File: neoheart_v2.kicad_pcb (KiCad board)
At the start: 2 copper layers, 54.2 x 46.5 mm, 45 parts, among them J1 Conn_01x03, Q1 A1SHB, Q2 BSS138, U2 TPS61240TDRVRQ1

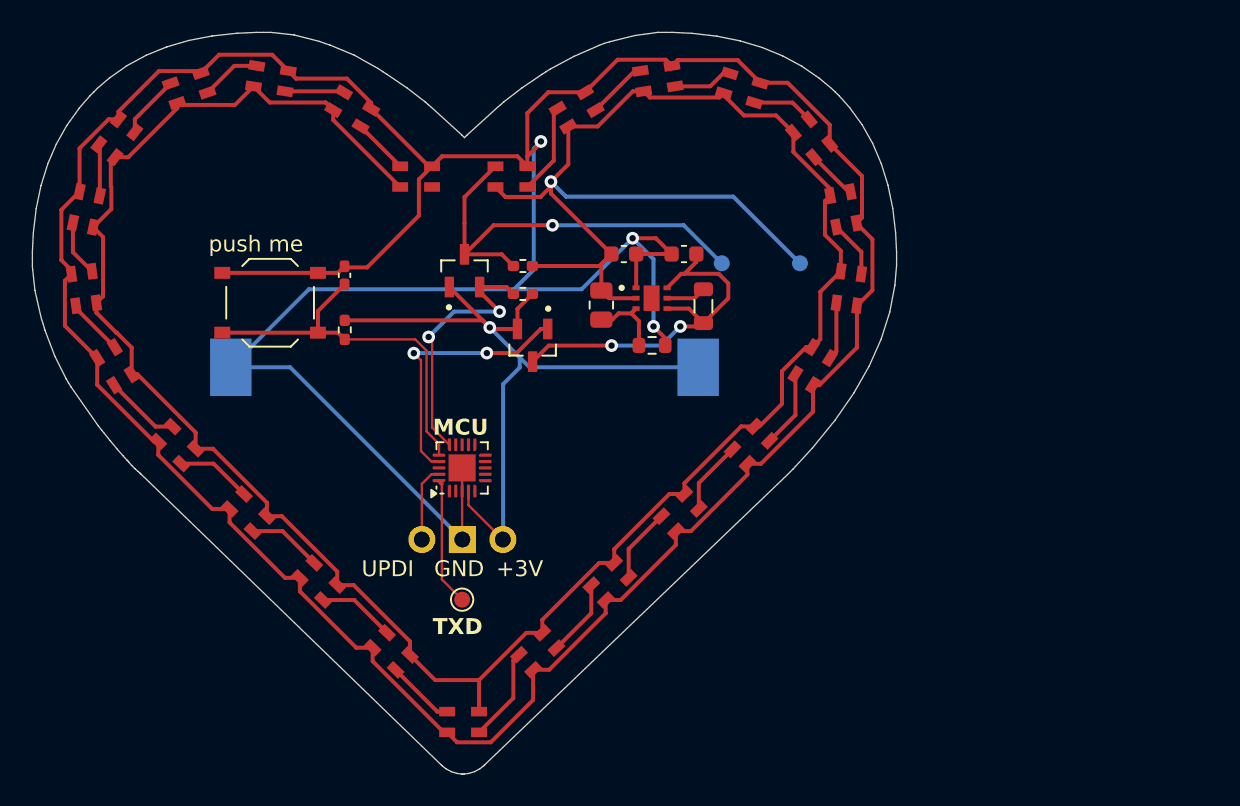
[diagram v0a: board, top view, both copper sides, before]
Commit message: 2.2: update schematic, new boost converter design, hardware optimizations
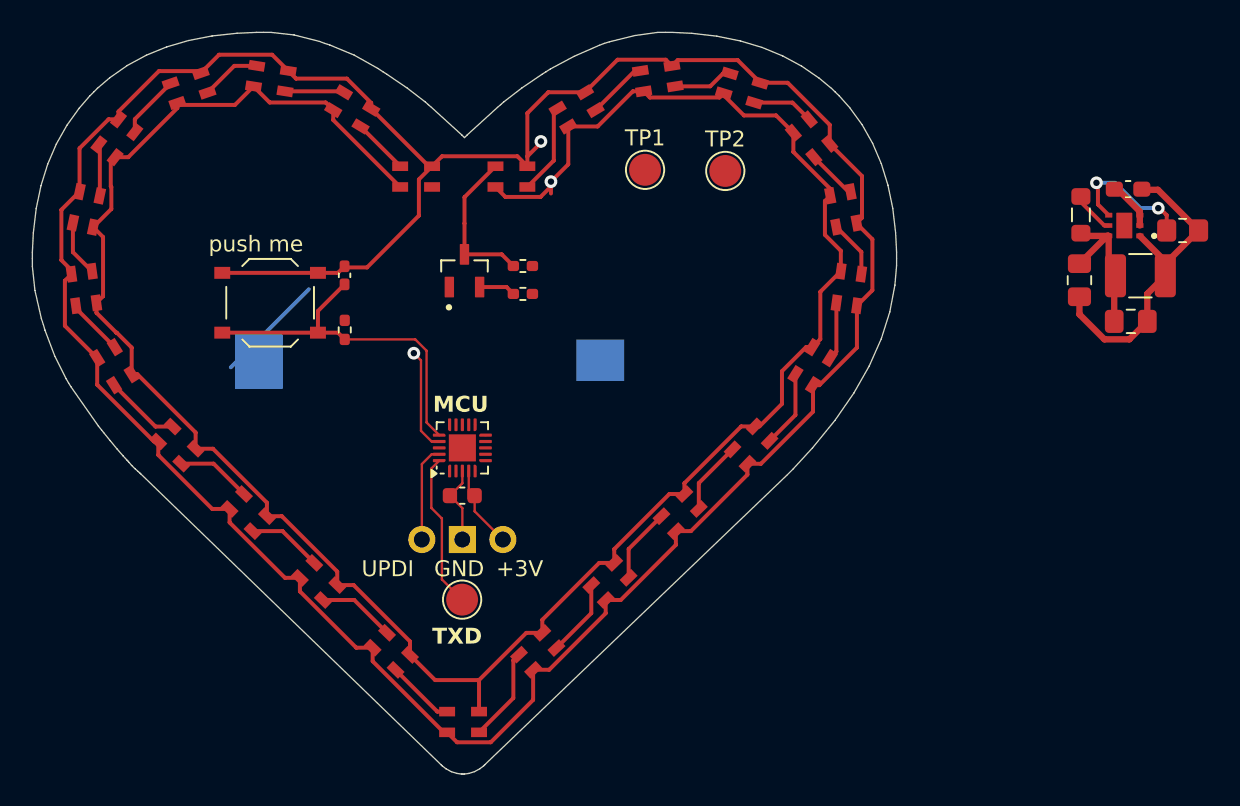
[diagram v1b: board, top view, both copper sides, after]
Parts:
- removed BT1: Battery, Battery:BatteryHolder_Keystone_1060_1x2032
- removed Q1: A1SHB, lib:SOT95P237X112-3N
- removed R2: 180kΩ, Resistor_SMD:R_0805_2012Metric
- removed R3: 1,5MΩ, Resistor_SMD:R_0603_1608Metric
- removed REF**: OSHW-Logo_5.7x6mm_SilkScreen, Symbol:OSHW-Logo_5.7x6mm_SilkScreen
- added C1: 100µF, Capacitor_SMD:C_1210_3225Metric_Pad1.33x2.70mm_HandSolder, F.Cu at (92.7, 41.4)
- added C5: 2.2µF, Capacitor_SMD:C_0805_2012Metric_Pad1.18x1.45mm_HandSolder, F.Cu at (92.1, 44.3)
- added C6: 100nF, Capacitor_SMD:C_0603_1608Metric, F.Cu at (50.2, 55.2)
- added J2: CR2032, lib:HARWIN_S8421-45R, B.Cu at (50.3, 46.7)
- added R6: 100K, Resistor_SMD:R_0805_2012Metric_Pad1.20x1.40mm_HandSolder, F.Cu at (95.3, 38.6)
- C3: footprint Capacitor_SMD:C_0603_1608Metric -> Capacitor_SMD:C_0805_2012Metric_Pad1.18x1.45mm_HandSolder
- C4: footprint Capacitor_SMD:C_0603_1608Metric -> Capacitor_SMD:C_0603_1608Metric_Pad1.08x0.95mm_HandSolder
- L1: value MLP2012V4R7MT0S1 -> 1μH; footprint Inductor_SMD:L_0805_2012Metric -> Inductor_SMD:L_0805_2012Metric_Pad1.05x1.20mm_HandSolder
- TP1, TP2: footprint TestPoint:TestPoint_Pad_D1.0mm -> TestPoint:TestPoint_Pad_D2.0mm; moved to F.Cu
- TP4: footprint TestPoint:TestPoint_Pad_D1.0mm -> TestPoint:TestPoint_Pad_D2.0mm
- U2: value TPS61240TDRVRQ1 -> TPS61240
- moved C4 31.9 mm to (91.9, 36.0)
- moved U2 30.0 mm to (91.7, 38.3), turned to 180 degrees
- moved C3 24.9 mm to (88.9, 41.7), turned to -90 degrees
- moved L1 24.4 mm to (89.0, 37.6)
- moved TP1 7.58 mm to (61.6, 34.8), turned to 0 degrees
- moved TP2 7.45 mm to (66.7, 34.9), turned to 0 degrees
- moved MCU1 1.26 mm to (50.2, 52.2)
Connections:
- C3 pad 1: /BOOST_3V0 -> +3V0
- L1 pad 1: /BOOST_3V0 -> +3V0
- MCU1 pad 17: /BOOST_MOSFET -> /BOOST_EN
- U2 pad 3: Net-(U2-FB) -> +5V
- U2 pad 4: /BOOST_3V0 -> /BOOST_EN
- U2 pad 6: /BOOST_3V0 -> +3V0
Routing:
- net GND: track 261.4 -> 210.4 mm, vias 3 -> 1
- net +5V: track 178.8 -> 148.6 mm
- net +3V0: track 50.6 -> 23.0 mm, vias 1 -> 0
- net /BOOST_3V0: track 23.6 -> 0.00 mm, vias 2 -> 0
- net /LED_DATA: track 27.7 -> 9.70 mm, vias 1 -> 0
- net /BOOST_MOSFET: track 16.8 -> 0.00 mm, vias 2 -> 0
- net /BOOST_EN: track 0.00 -> 15.0 mm, vias 0 -> 3
- net /IO_LEDS: track 16.8 -> 2.29 mm, vias 2 -> 0
- net Net-(U2-FB): track 4.67 -> 0.00 mm
- net /TX: track 8.04 -> 9.72 mm
- net /UPDI: track 4.81 -> 6.07 mm
- net /SW_ANIM: track 23.9 -> 22.6 mm
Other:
- board text removed: "JLCJLCJLCJLC"

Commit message: 2.2: update PCB, add production files, new board renders
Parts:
- added REF**: OSHW-Logo_5.7x6mm_SilkScreen, Symbol:OSHW-Logo_5.7x6mm_SilkScreen, B.Cu at (50.3, 67.2)
- TP1, TP2: footprint TestPoint:TestPoint_Pad_D2.0mm -> TestPoint:TestPoint_Pad_D1.5mm; moved to B.Cu
- TP4: footprint TestPoint:TestPoint_Pad_D2.0mm -> TestPoint:TestPoint_Pad_D1.5mm
- moved R6 35.5 mm to (59.9, 39.9), turned to 90 degrees
- moved C4 35.4 mm to (57.3, 43.3), turned to 90 degrees
- moved U2 32.5 mm to (59.6, 43.5), turned to -90 degrees
- moved L1 31.3 mm to (58.9, 46.2), turned to 180 degrees
- moved C1 30.0 mm to (62.8, 42.5), turned to 90 degrees
- moved C5 26.5 mm to (65.6, 43.1), turned to 90 degrees
- moved C3 26.3 mm to (63.0, 46.3), turned to 0 degrees
- moved TP1 8.09 mm to (68.0, 39.7), turned to 180 degrees
- moved TP2 7.09 mm to (71.8, 39.7), turned to 180 degrees
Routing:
- net GND: track 210.4 -> 9.77 mm, vias 1 -> 18
- net +3V0: track 23.0 -> 70.9 mm, vias 0 -> 2
- net +5V: track 148.6 -> 175.9 mm
- net /LED_DATA: track 9.70 -> 29.2 mm, vias 0 -> 1
- net /BOOST_EN: track 15.0 -> 25.7 mm
- net /IO_LEDS: track 2.29 -> 11.7 mm
- added copper zone on B.Cu, net GND
- added copper zone on F.Cu, net GND
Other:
- board text added: "HEART V2.2"
- board text added: "NEO"
- board text added: "WAYWAYWAY"
- board text removed: "DEBUG:"
- board text removed: "NEOHEART V2.1"
